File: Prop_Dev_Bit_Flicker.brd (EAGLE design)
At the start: 63.2 x 24.9 mm, 71 parts, among them J1 MF-CON-MICROUSB-RIGHT, J4 M20-7822046, J5 M20-7822046, U1 P8X32A-Q44, U2 FT230XQ-R, U3 TPS2113ADRBR, U4 CAT24C512WI-GT3, U5 MAX11613EUA+, U6 NCP1117LPST33T3G, U7 IRLML6401TRPBF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

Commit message: Fixed part number for Prop to P8X32A-M44
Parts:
- U1: value P8X32A-Q44 -> P8X32A-M44
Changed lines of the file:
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@@
 <attribute name="NAME" x="14.631" y="19.872" size="0.8128" layer="21" font="vector"/>
 </element>
-<element name="U1" library="PP_DigitalIC" package="P8X32A_QFN-44" value="P8X32A-Q44" x="28.702" y="12.192" smashed="yes" rot="R90">
+<element name="U1" library="PP_DigitalIC" package="P8X32A_QFN-44" value="P8X32A-M44" x="28.702" y="12.192" smashed="yes" rot="R90">
 <attribute name="NAME" x="23.552" y="5.908" size="0.8128" layer="25" font="vector"/>
 </element>

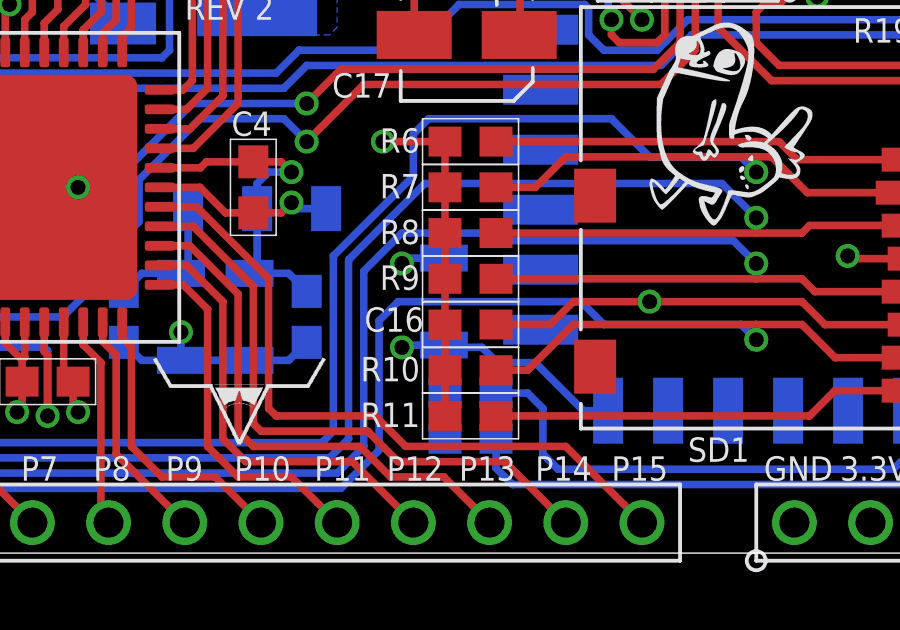
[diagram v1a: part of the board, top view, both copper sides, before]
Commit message: New Camfiles and added Tant Cap 100uF to 3.3V
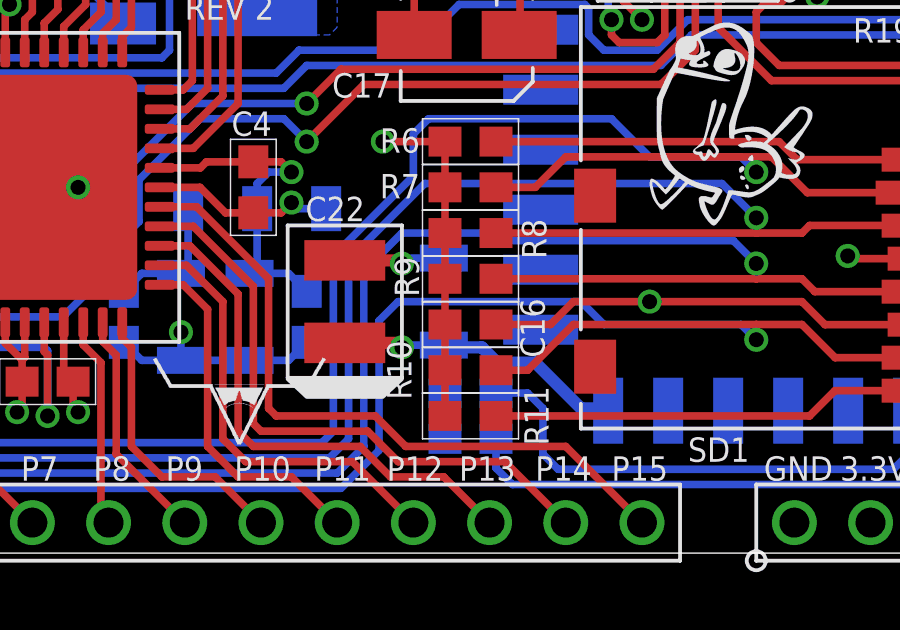
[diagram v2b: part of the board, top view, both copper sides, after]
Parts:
- added C22: F930J107MBA, PP_Passives:CASE_B
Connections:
- net 3.3V: now also C22.P
- net GND: now also C22.N
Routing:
- net 3.3V: track 85.1 -> 87.1 mm
- net GND: track 141.8 -> 143.8 mm
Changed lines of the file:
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@@
 </element>
 <element name="R8" library="PP_Passives" package="0603" value="10K" x="43.561" y="10.668" smashed="yes" rot="R180">
-<attribute name="NAME" x="41.875" y="11.1125" size="0.8128" layer="25" font="vector" rot="R180"/>
+<attribute name="NAME" x="45.2755" y="11.141" size="0.8128" layer="25" font="vector" rot="R270"/>
 </element>
 <element name="R9" library="PP_Passives" package="0603" value="10K" x="43.561" y="9.144" smashed="yes" rot="R180">
-<attribute name="NAME" x="41.875" y="9.5885" size="0.8128" layer="25" font="vector" rot="R180"/>
+<attribute name="NAME" x="41.8465" y="8.544" size="0.8128" layer="25" font="vector" rot="R90"/>
 </element>
 <element name="R10" library="PP_Passives" package="0603" value="10K" x="43.561" y="6.096" smashed="yes" rot="R180">
-<attribute name="NAME" x="41.875" y="6.5405" size="0.8128" layer="25" font="vector" rot="R180"/>
+<attribute name="NAME" x="41.5925" y="5.115" size="0.8128" layer="25" font="vector" rot="R90"/>
 </element>
 <element name="R11" library="PP_Passives" package="0603" value="10K" x="43.561" y="4.572" smashed="yes" rot="R180">
-<attribute name="NAME" x="41.875" y="5.0165" size="0.8128" layer="25" font="vector" rot="R180"/>
+<attribute name="NAME" x="46.1645" y="3.591" size="0.8128" layer="25" font="vector" rot="R90"/>
 </element>
 <element name="C16" library="PP_Passives" package="0603" value=".1uF" x="43.561" y="7.62" smashed="yes">
-<attribute name="NAME" x="42.002" y="8.1915" size="0.8128" layer="25" font="vector" rot="R180"/>
+<attribute name="NAME" x="46.0375" y="6.512" size="0.8128" layer="25" font="vector" rot="R90"/>
 </element>
 <element name="R14" library="PP_Passives" package="0603" value="10K" x="16.129" y="5.588" smashed="yes" rot="R180">
@@
 <element name="PROG" library="PP_Electromechanical" package="EVPBB" value="EVP-BB2A1B000" x="60.96" y="20.066" smashed="yes">
 <attribute name="NAME" x="56.566" y="20.685" size="0.8128" layer="25" font="vector"/>
+</element>
+<element name="C22" library="PP_Passives" package="CASE_B" value="F930J107MBA" x="39.37" y="8.382" smashed="yes" rot="R90">
+<attribute name="NAME" x="38.06" y="11.065" size="0.8128" layer="21" font="vector"/>
 </element>
 </elements>
@@
 <wire x1="62.285" y1="19.691" x2="62.285" y2="17.76475" width="0.254" layer="1"/>
 <wire x1="62.285" y1="17.76475" x2="61.86525" y2="17.76475" width="0.254" layer="1"/>
+<contactref element="C22" pad="N"/>
+<wire x1="39.37" y1="9.757" x2="41.17" y2="9.757" width="0.4064" layer="1"/>
+<wire x1="41.17" y1="9.757" x2="41.275" y2="9.652" width="0.4064" layer="1"/>
 </signal>
 <signal name="SDA">
@@
 <wire x1="42.672" y1="5.373" x2="42.711" y2="5.334" width="0.254" layer="16"/>
 <wire x1="42.711" y1="3.81" x2="42.711" y2="5.334" width="0.254" layer="16"/>
-<wire x1="48.15" y1="4.746" x2="47.324" y2="4.746" width="0.254" layer="16"/>
-<wire x1="47.324" y1="4.746" x2="45.72" y2="6.35" width="0.254" layer="16"/>
-<wire x1="45.72" y1="6.35" x2="44.45" y2="6.35" width="0.254" layer="16"/>
-<wire x1="44.45" y1="6.35" x2="43.942" y2="6.858" width="0.254" layer="16"/>
-<wire x1="43.942" y1="6.858" x2="42.746" y2="6.858" width="0.254" layer="16"/>
 <wire x1="42.746" y1="6.858" x2="42.672" y2="6.932" width="0.254" layer="16"/>
 <wire x1="42.672" y1="6.932" x2="41.349" y2="6.932" width="0.254" layer="16"/>
@@
 <wire x1="55.118" y1="19.304" x2="55.118" y2="18.542" width="0.254" layer="1"/>
 <via x="55.118" y="18.542" extent="1-16" drill="0.5"/>
+<contactref element="C22" pad="P"/>
+<wire x1="39.37" y1="7.007" x2="41.126" y2="7.007" width="0.4064" layer="1"/>
+<wire x1="41.126" y1="7.007" x2="41.275" y2="6.858" width="0.4064" layer="1"/>
+<wire x1="42.746" y1="6.858" x2="43.942" y2="6.858" width="0.4064" layer="16"/>
+<wire x1="43.942" y1="6.858" x2="44.45" y2="6.35" width="0.4064" layer="16"/>
+<wire x1="44.45" y1="6.35" x2="45.72" y2="6.35" width="0.4064" layer="16"/>
+<wire x1="45.72" y1="6.35" x2="47.244" y2="4.826" width="0.4064" layer="16"/>
+<wire x1="47.244" y1="4.826" x2="48.07" y2="4.826" width="0.4064" layer="16"/>
+<wire x1="48.07" y1="4.826" x2="48.15" y2="4.746" width="0.4064" layer="16"/>
 </signal>
 <signal name="SD_SCLK">

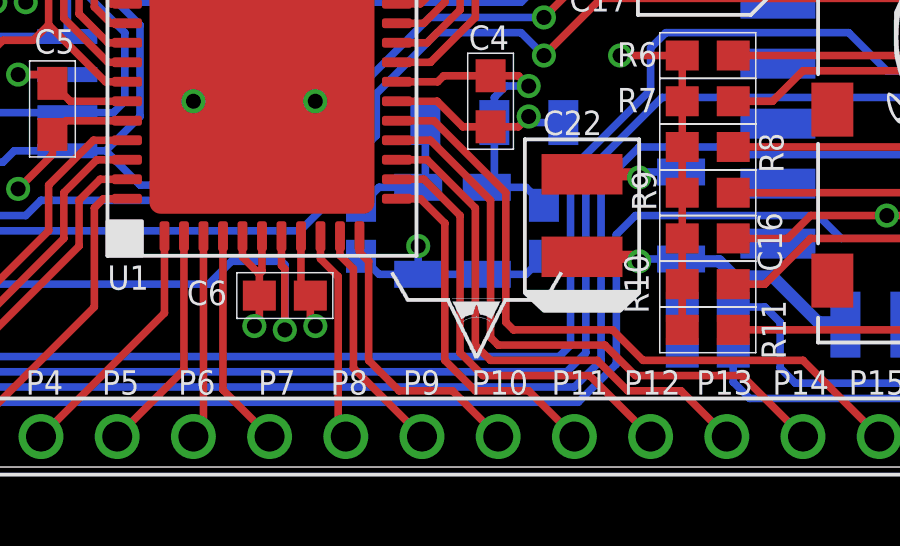
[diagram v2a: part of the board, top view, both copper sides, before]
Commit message: Fixed silkscreen on top. Moved LHE Logo.
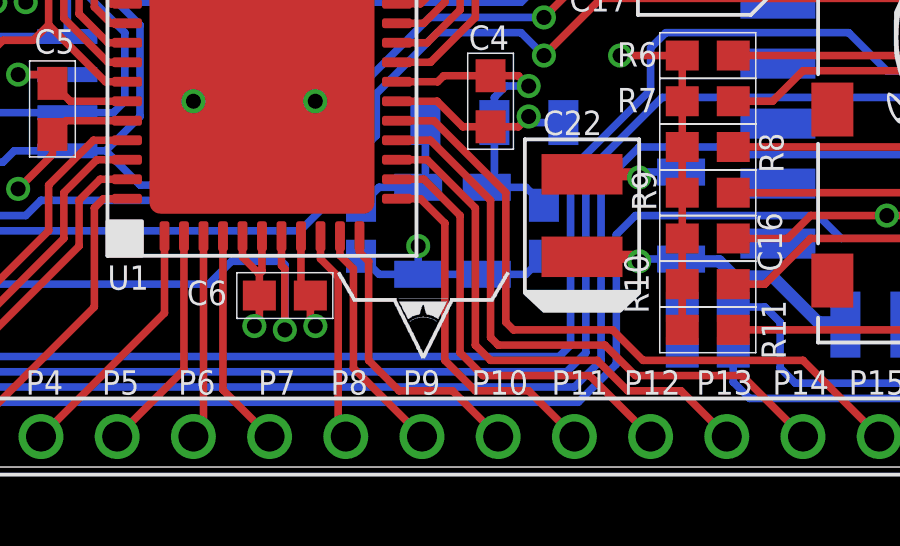
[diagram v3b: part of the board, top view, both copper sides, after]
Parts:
- moved U$2 1.78 mm to (36.1, 3.56)
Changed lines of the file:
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@@
 <attribute name="NAME" x="11.338" y="18.0975" size="0.8128" layer="26" font="vector" rot="MR180"/>
 </element>
-<element name="U$2" library="PP_Aesthetics" package="LHE_LOGO" value="LHE_LOGOLHE_LOGO" x="37.846" y="3.556"/>
+<element name="U$2" library="PP_Aesthetics" package="LHE_LOGO" value="LHE_LOGOLHE_LOGO" x="36.068" y="3.556"/>
 <element name="C14" library="PP_Passives" package="0603" value=".1uF" x="46.609" y="20.066" smashed="yes" rot="R90">
 <attribute name="NAME" x="45.558" y="21.1455" size="0.8128" layer="25" font="vector" rot="R180"/>
